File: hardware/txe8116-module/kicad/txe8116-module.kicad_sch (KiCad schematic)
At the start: 0 parts

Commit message: Add SMD resistor footprint and update schematic symbols for R_Small
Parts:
- added R1: R_Small, Resistor_SMD:R_0805_2012Metric, symbol Device:R_Small
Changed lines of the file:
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@@
 	(generator_version "9.0")
 	(paper "A4")
+	(symbol
+		(lib_id "Device:R_Small")
+		(at 134.62 72.39 0)
+		(unit 1)
+		(exclude_from_sim no)
+		(in_bom yes)
+		(on_board yes)
+		(dnp no)
+		(fields_autoplaced yes)
+		(property "Reference" "R1"
+			(at 137.16 71.1199 0)
+			(effects
+				(font
+					(size 1.016 1.016)
+				)
+				(justify left)
+			)
+		)
+		(property "Value" "R_Small"
+			(at 137.16 73.6599 0)
+			(effects
+				(font
+					(size 1.27 1.27)
+				)
+				(justify left)
+			)
+		)
+		(property "Footprint" "Resistor_SMD:R_0805_2012Metric"
+			(at 134.62 72.39 0)
+			(effects
+				(font
+					(size 1.27 1.27)
+				)
+				(hide yes)
+			)
+		)
+		(property "Datasheet" "~"
+			(at 134.62 72.39 0)
+			(effects
+				(font
+					(size 1.27 1.27)
+				)
+				(hide yes)
+			)
+		)
+		(property "Description" "Resistor, small symbol"
+			(at 134.62 72.39 0)
+			(effects
+				(font
+					(size 1.27 1.27)
+				)
+				(hide yes)
+			)
+		)
+		(pin "1"
+		)
+		(pin "2"
+		)
+		(instances
+			(project ""
+				(path "/07123eb2-095c-4276-b37d-21a84783f032"
+					(reference "R1")
+					(unit 1)
+				)
+			)
+		)
+	)
 	(sheet_instances
 		(path "/"

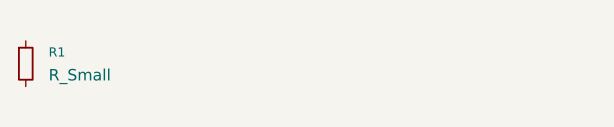
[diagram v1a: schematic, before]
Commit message: Add screw terminal footprint and update schematic
- Introduced a new screw terminal footprint (WAGO 2601-1102) in the PCB layout.
- Updated net connections for the new terminal block.
- Modified the resistor value in the schematic to 100k.
- Added a new connector symbol for the screw terminal in the schematic.
- Enhanced the schematic with additional wire connections for better clarity.
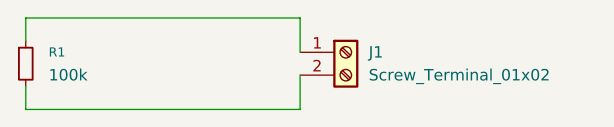
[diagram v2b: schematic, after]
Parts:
- added J1: Screw_Terminal_01x02, TerminalBlock_WAGO:TerminalBlock_WAGO_2601-1102_1x02_P3.50mm_Horizontal, symbol Connector:Screw_Terminal_01x02
- R1: value R_Small -> 100k
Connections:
- net at R1.1: now also J1.1 (Pin_1)
- net at R1.2: now also J1.2 (Pin_2)
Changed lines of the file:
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@@
 	(generator_version "9.0")
 	(paper "A4")
+	(wire
+		(pts
+			(xy 134.62 69.85) (xy 134.62 67.31)
+		)
+		(stroke
+			(width 0)
+			(type default)
+		)
+	)
+	(wire
+		(pts
+			(xy 165.1 73.66) (xy 165.1 77.47)
+		)
+		(stroke
+			(width 0)
+			(type default)
+		)
+	)
+	(wire
+		(pts
+			(xy 165.1 77.47) (xy 134.62 77.47)
+		)
+		(stroke
+			(width 0)
+			(type default)
+		)
+	)
+	(wire
+		(pts
+			(xy 165.1 67.31) (xy 165.1 71.12)
+		)
+		(stroke
+			(width 0)
+			(type default)
+		)
+	)
+	(wire
+		(pts
+			(xy 134.62 74.93) (xy 134.62 77.47)
+		)
+		(stroke
+			(width 0)
+			(type default)
+		)
+	)
+	(wire
+		(pts
+			(xy 134.62 67.31) (xy 165.1 67.31)
+		)
+		(stroke
+			(width 0)
+			(type default)
+		)
+	)
+	(symbol
+		(lib_id "Connector:Screw_Terminal_01x02")
+		(at 170.18 71.12 0)
+		(unit 1)
+		(exclude_from_sim no)
+		(in_bom yes)
+		(on_board yes)
+		(dnp no)
+		(fields_autoplaced yes)
+		(property "Reference" "J1"
+			(at 172.72 71.1199 0)
+			(effects
+				(font
+					(size 1.27 1.27)
+				)
+				(justify left)
+			)
+		)
+		(property "Value" "Screw_Terminal_01x02"
+			(at 172.72 73.6599 0)
+			(effects
+				(font
+					(size 1.27 1.27)
+				)
+				(justify left)
+			)
+		)
+		(property "Footprint" "TerminalBlock_WAGO:TerminalBlock_WAGO_2601-1102_1x02_P3.50mm_Horizontal"
+			(at 170.18 71.12 0)
+			(effects
+				(font
+					(size 1.27 1.27)
+				)
+				(hide yes)
+			)
+		)
+		(property "Datasheet" "~"
+			(at 170.18 71.12 0)
+			(effects
+				(font
+					(size 1.27 1.27)
+				)
+				(hide yes)
+			)
+		)
+		(property "Description" "Generic screw terminal, single row, 01x02, script generated (kicad-library-utils/schlib/autogen/connector/)"
+			(at 170.18 71.12 0)
+			(effects
+				(font
+					(size 1.27 1.27)
+				)
+				(hide yes)
+			)
+		)
+		(pin "1"
+		)
+		(pin "2"
+		)
+		(instances
+			(project ""
+				(path "/07123eb2-095c-4276-b37d-21a84783f032"
+					(reference "J1")
+					(unit 1)
+				)
+			)
+		)
+	)
 	(symbol
 		(lib_id "Device:R_Small")
@@
 			)
 		)
-		(property "Value" "R_Small"
+		(property "Value" "100k"
 			(at 137.16 73.6599 0)
 			(effects

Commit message: Added some components
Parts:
- added U1: TXE8116, txe8116:Texas_DGS0024A_TSSOP-24_3x6.1mm_P0.5mm, symbol txe8116:TXE8116
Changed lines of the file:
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@@
+		)
+	)
+	(symbol
+		(lib_id "txe8116:TXE8116")
+		(at 120.65 111.76 0)
+		(unit 1)
+		(exclude_from_sim no)
+		(in_bom yes)
+		(on_board yes)
+		(dnp no)
+		(fields_autoplaced yes)
+		(property "Reference" "U1"
+			(at 122.7933 85.09 0)
+			(effects
+				(font
+					(size 1.27 1.27)
+				)
+				(justify left)
+			)
+		)
+		(property "Value" "TXE8116"
+			(at 122.7933 87.63 0)
+			(effects
+				(font
+					(size 1.27 1.27)
+				)
+				(justify left)
+			)
+		)
+		(property "Footprint" "txe8116:Texas_DGS0024A_TSSOP-24_3x6.1mm_P0.5mm"
+			(at 120.65 111.76 0)
+			(effects
+				(font
+					(size 1.27 1.27)
+				)
+				(hide yes)
+			)
+		)
+		(property "Datasheet" "https://www.ti.com/lit/ds/symlink/txe8116.pdf"
+			(at 120.65 111.76 0)
+			(effects
+				(font
+					(size 1.27 1.27)
+				)
+				(hide yes)
+			)
+		)
+		(property "Description" "16-Bit SPI Bus I/O Expander with Interrupt Output, Reset Input"
+			(at 120.65 111.76 0)
+			(effects
+				(font
+					(size 1.27 1.27)
+				)
+				(hide yes)
+			)
+		)
+		(pin "4"
+		)
+		(pin "6"
+		)
+		(pin "1"
+		)
+		(pin "2"
+		)
+		(pin "24"
+		)
+		(pin "22"
+		)
+		(pin "21"
+		)
+		(pin "3"
+		)
+		(pin "23"
+		)
+		(pin "5"
+		)
+		(pin "19"
+		)
+		(pin "16"
+		)
+		(pin "18"
+		)
+		(pin "15"
+		)
+		(pin "14"
+		)
+		(pin "10"
+		)
+		(pin "12"
+		)
+		(pin "17"
+		)
+		(pin "7"
+		)
+		(pin "13"
+		)
+		(pin "8"
+		)
+		(pin "20"
+		)
+		(pin "9"
+		)
+		(pin "11"
+		)
+		(instances
+			(project ""
+				(path "/07123eb2-095c-4276-b37d-21a84783f032"
+					(reference "U1")
+					(unit 1)
+				)
+			)
 		)
 	)

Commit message: Refactor code structure for improved readability and maintainability
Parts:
- removed J1: Screw_Terminal_01x02, TerminalBlock_WAGO:TerminalBlock_WAGO_2601-1102_1x02_P3.50mm_Horizontal, symbol Connector:Screw_Terminal_01x02
- removed R1: 100k, Resistor_SMD:R_0805_2012Metric, symbol Device:R_Small
- added C3: 0u1, Capacitor_SMD:C_0603_1608Metric, symbol Device:C_Small
- added C4: 4u7, Capacitor_SMD:C_0603_1608Metric, symbol Device:C_Small
- added D1, D10, D11, D12, D13, D14, D15, D16, D17, D18, D19, D2, D20, D21, D22, D23, D3, D4, D5, D6, D7, D8, D9: ESD9B5.0ST5G, Diode_SMD:D_SOD-923, symbol Diode:ESD9B5.0ST5G
- added J1: Conn_01x12, misc:1x12_P2.54mm_Castellated_Mirrored, symbol Connector_Generic:Conn_01x12
- added J2: Conn_01x12, misc:1x12_P2.54mm_Castellated, symbol Connector_Generic:Conn_01x12
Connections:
- net ~{INT}: now reaches U1.1 (~{INT})
- net ~{INT}: now also D2.1 (A1), J1.2 (Pin_2)
- net GPIO0.5: now reaches U1.10 (P0.5)
- net GPIO0.5: now also D8.1 (A1), J1.8 (Pin_8)
- net GPIO0.6: now reaches U1.11 (P0.6)
- net GPIO0.6: now also D9.1 (A1), J1.9 (Pin_9)
- net GPIO0.7: now reaches U1.12 (P0.7)
- net GPIO0.7: now also D10.1 (A1), J1.10 (Pin_10)
- net GPIO1.7: now reaches U1.13 (P1.7)
- net GPIO1.7: now also D23.1 (A1), J2.11 (Pin_11)
- net GPIO1.6: now reaches U1.14 (P1.6)
- net GPIO1.6: now also D22.1 (A1), J2.10 (Pin_10)
- net GPIO1.5: now reaches U1.15 (P1.5)
- net GPIO1.5: now also D21.1 (A1), J2.9 (Pin_9)
- net GPIO1.4: now reaches U1.16 (P1.4)
- net GPIO1.4: now also D20.1 (A1), J2.8 (Pin_8)
- net GPIO1.3: now reaches U1.17 (P1.3)
- net GPIO1.3: now also D19.1 (A1), J2.7 (Pin_7)
- net GPIO1.2: now reaches U1.18 (P1.2)
- net GPIO1.2: now also D18.1 (A1), J2.6 (Pin_6)
- net GPIO1.1: now reaches U1.19 (P1.1)
- net GPIO1.1: now also D12.1 (A1), J1.12 (Pin_12)
- net SDO: now reaches U1.2 (SDO)
- net SDO: now also D14.1 (A1), J2.2 (Pin_2)
- net GPIO1.0: now reaches U1.20 (P1.0)
- net GPIO1.0: now also D11.1 (A1), J1.11 (Pin_11)
- net ~{CS}: now reaches U1.21 (~{CS})
- net ~{CS}: now also D17.1 (A1), J2.5 (Pin_5)
- net SCLK: now reaches U1.22 (SCLK)
- net SCLK: now also D16.1 (A1), J2.4 (Pin_4)
- net SDI: now reaches U1.23 (SDI)
- net SDI: now also D15.1 (A1), J2.3 (Pin_3)
- net ~{RESET}: now reaches U1.24 (~{RESET})
- net ~{RESET}: now also D13.1 (A1), J2.1 (Pin_1)
- net VCC: now reaches U1.3 (VCC)
- net VCC: now also C3.1, C4.1, D1.1 (A1), J1.1 (Pin_1)
- net GND: now reaches U1.4 (GND)
- net GND: now also C3.2, C4.2, D1.2 (A2), D10.2 (A2), D11.2 (A2), D12.2 (A2), D13.2 (A2), D14.2 (A2), D15.2 (A2), D16.2 (A2), D17.2 (A2), D18.2 (A2), D19.2 (A2), D2.2 (A2), D20.2 (A2), D21.2 (A2), D22.2 (A2), D23.2 (A2), D3.2 (A2), D4.2 (A2), D5.2 (A2), D6.2 (A2), D7.2 (A2), D8.2 (A2), D9.2 (A2), J2.12 (Pin_12)
- net GPIO0.0: now reaches U1.5 (P0.0)
- net GPIO0.0: now also D3.1 (A1), J1.3 (Pin_3)
- net GPIO0.1: now reaches U1.6 (P0.1)
- net GPIO0.1: now also D4.1 (A1), J1.4 (Pin_4)
- net GPIO0.2: now reaches U1.7 (P0.2)
- net GPIO0.2: now also D5.1 (A1), J1.5 (Pin_5)
- net GPIO0.3: now reaches U1.8 (P0.3)
- net GPIO0.3: now also D6.1 (A1), J1.6 (Pin_6)
- net GPIO0.4: now reaches U1.9 (P0.4)
- net GPIO0.4: now also D7.1 (A1), J1.7 (Pin_7)
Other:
- moved on the sheet: U1

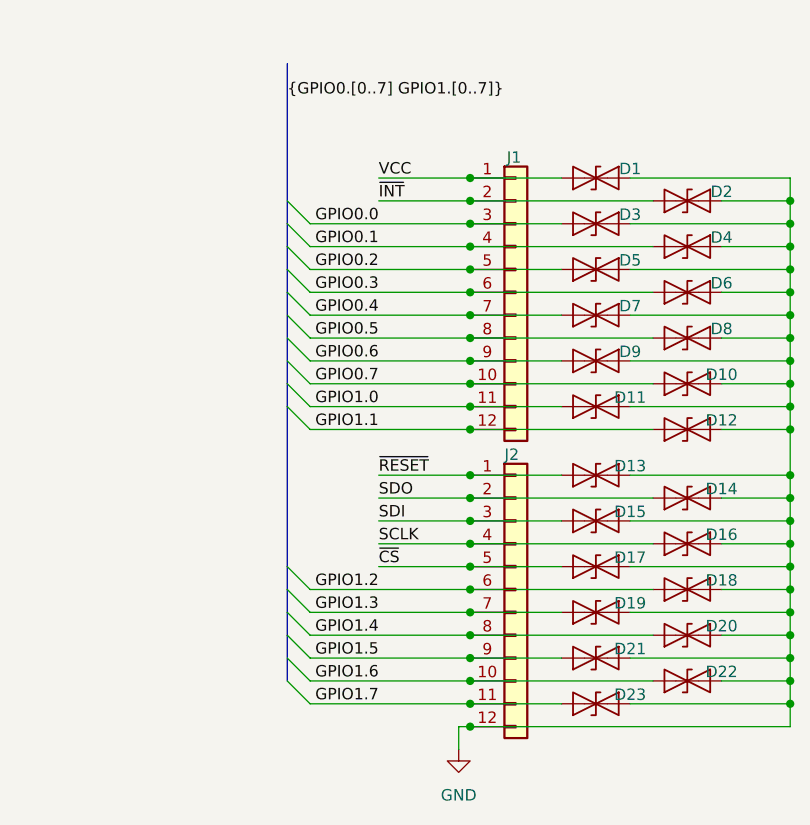
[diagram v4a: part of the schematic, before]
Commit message: Add PWR_FLAG symbols to indicate power source for ERC checks
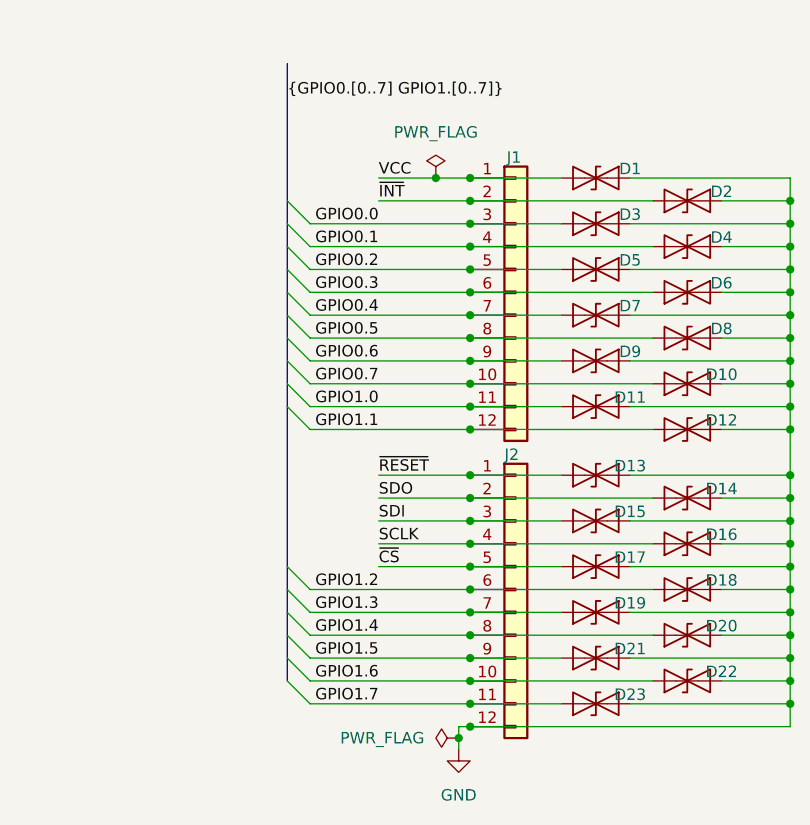
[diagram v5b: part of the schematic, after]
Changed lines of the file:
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@@
+	)
+	(junction
+		(at 201.93 38.1)
+		(diameter 0)
+		(color 0 0 0 0)
 	)
 	(junction
@@
 	(junction
 		(at 205.74 86.36)
+		(diameter 0)
+		(color 0 0 0 0)
+	)
+	(junction
+		(at 204.47 100.33)
 		(diameter 0)
 		(color 0 0 0 0)
@@
 	(wire
 		(pts
+			(xy 201.93 38.1) (xy 205.74 38.1)
+		)
+		(stroke
+			(width 0)
+			(type default)
+		)
+	)
+	(wire
+		(pts
 			(xy 36.83 43.18) (xy 45.72 43.18)
 		)
@@
 	(wire
 		(pts
-			(xy 195.58 38.1) (xy 205.74 38.1)
+			(xy 195.58 38.1) (xy 201.93 38.1)
 		)
 		(stroke
@@
 	(wire
 		(pts
-			(xy 204.47 99.06) (xy 204.47 101.6)
+			(xy 204.47 99.06) (xy 204.47 100.33)
 		)
 		(stroke
@@
 		(pts
 			(xy 83.82 43.18) (xy 83.82 45.72)
+		)
+		(stroke
+			(width 0)
+			(type default)
+		)
+	)
+	(wire
+		(pts
+			(xy 204.47 100.33) (xy 204.47 101.6)
 		)
 		(stroke
@@
 	)
 	(symbol
+		(lib_id "power:PWR_FLAG")
+		(at 204.47 100.33 90)
+		(unit 1)
+		(exclude_from_sim no)
+		(in_bom yes)
+		(on_board yes)
+		(dnp no)
+		(fields_autoplaced yes)
+		(property "Reference" "#FLG02"
+			(at 202.565 100.33 0)
+			(effects
+				(font
+					(size 1.27 1.27)
+				)
+				(hide yes)
+			)
+		)
+		(property "Value" "PWR_FLAG"
+			(at 200.66 100.3299 90)
+			(effects
+				(font
+					(size 1.27 1.27)
+				)
+				(justify left)
+			)
+		)
+		(property "Footprint" ""
+			(at 204.47 100.33 0)
+			(effects
+				(font
+					(size 1.27 1.27)
+				)
+				(hide yes)
+			)
+		)
+		(property "Datasheet" "~"
+			(at 204.47 100.33 0)
+			(effects
+				(font
+					(size 1.27 1.27)
+				)
+				(hide yes)
+			)
+		)
+		(property "Description" "Special symbol for telling ERC where power comes from"
+			(at 204.47 100.33 0)
+			(effects
+				(font
+					(size 1.27 1.27)
+				)
+				(hide yes)
+			)
+		)
+		(pin "1"
+		)
+		(instances
+			(project ""
+				(path "/07123eb2-095c-4276-b37d-21a84783f032"
+					(reference "#FLG02")
+					(unit 1)
+				)
+			)
+		)
+	)
+	(symbol
 		(lib_id "Device:C_Small")
 		(at 39.37 66.04 0)
@@
 					(unit 1)
 				)
+			)
+		)
+	)
+	(symbol
+		(lib_id "power:PWR_FLAG")
+		(at 201.93 38.1 0)
+		(unit 1)
+		(exclude_from_sim no)
+		(in_bom yes)
+		(on_board yes)
+		(dnp no)
+		(fields_autoplaced yes)
+		(property "Reference" "#FLG01"
+			(at 201.93 36.195 0)
+			(effects
+				(font
+					(size 1.27 1.27)
+				)
+				(hide yes)
+			)
+		)
+		(property "Value" "PWR_FLAG"
+			(at 201.93 33.02 0)
+			(effects
+				(font
+					(size 1.27 1.27)
+				)
+			)
+		)
+		(property "Footprint" ""
+			(at 201.93 38.1 0)
+			(effects
+				(font
+					(size 1.27 1.27)
+				)
+				(hide yes)
+			)
+		)
+		(property "Datasheet" "~"
+			(at 201.93 38.1 0)
+			(effects
+				(font
+					(size 1.27 1.27)
+				)
+				(hide yes)
+			)
+		)
+		(property "Description" "Special symbol for telling ERC where power comes from"
+			(at 201.93 38.1 0)
+			(effects
+				(font
+					(size 1.27 1.27)
+				)
+				(hide yes)
+			)
+		)
+		(pin "1"
+		)
+		(instances
+			(project ""
+				(path "/07123eb2-095c-4276-b37d-21a84783f032"
+					(reference "#FLG01")
+					(unit 1)
+				)

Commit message: Refactor netclass assignments and update component properties for improved clarity
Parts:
- D1, D10, D11, D12, D13, D14, D15, D16, D17, D18, D19, D2, D20, D21, D22, D23, D3, D4, D5, D6, D7, D8, D9: MFG (none) -> OnSemi; MPN (none) -> ESD9B5.0ST5G; OC_LCSC (none) -> C111566
- J1, J2: now left out of the parts list
- U1: MFG (none) -> Texas Instruments; MPN (none) -> TXE8116DGSR; OC_LCSC (none) -> C50498576

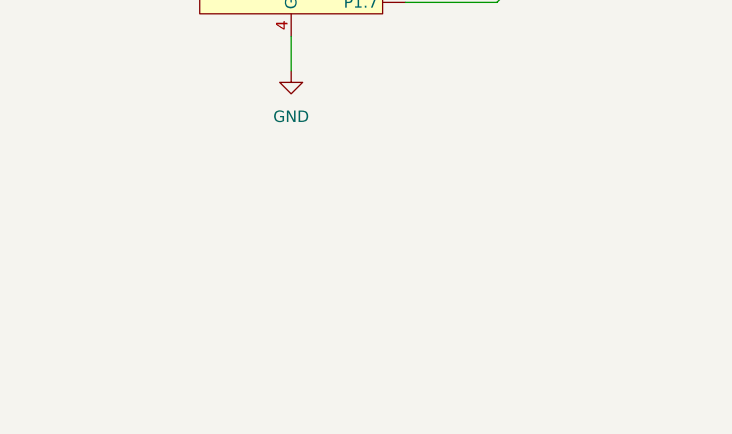
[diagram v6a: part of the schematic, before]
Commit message: fix(hardware): add 10k pull-up resistors on RESET and INT per datasheet
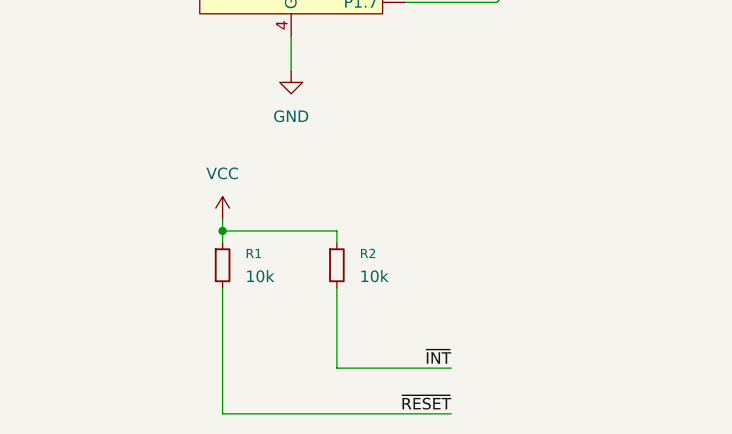
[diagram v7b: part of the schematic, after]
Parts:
- added R1, R2: 10k, Resistor_SMD:R_0603_1608Metric, symbol Device:R_Small
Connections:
- net VCC: now also R1.1, R2.1
- net ~{INT}: now also R2.2
- net ~{RESET}: now also R1.2
